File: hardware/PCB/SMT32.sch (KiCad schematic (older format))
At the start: 24 parts, among them J1 USB_B_Micro, SW1 SW_DIP_x01, SW2 SW_DIP_x01, U3 AZ1117CH-3.3, U4 STM32F303CCTx, Y1 X50328MSB2GI

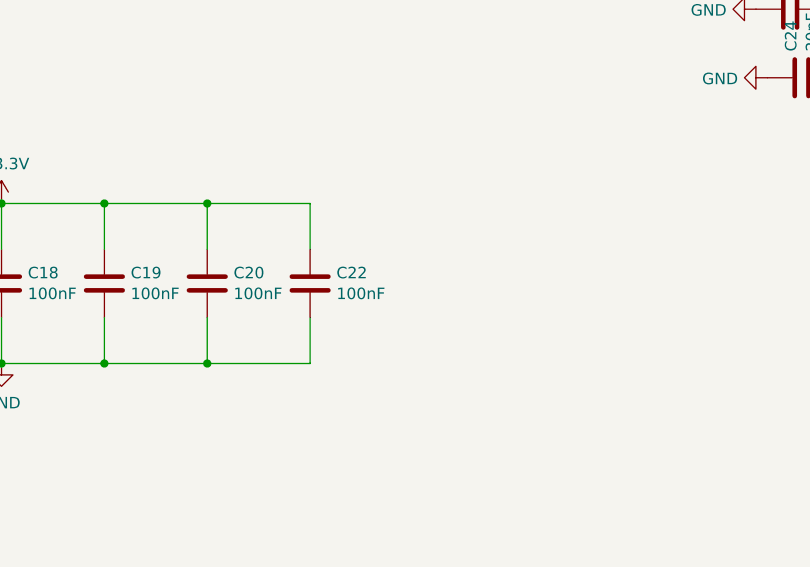
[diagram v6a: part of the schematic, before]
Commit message: Rotate the RGB controller. gonna have a lot of work to do
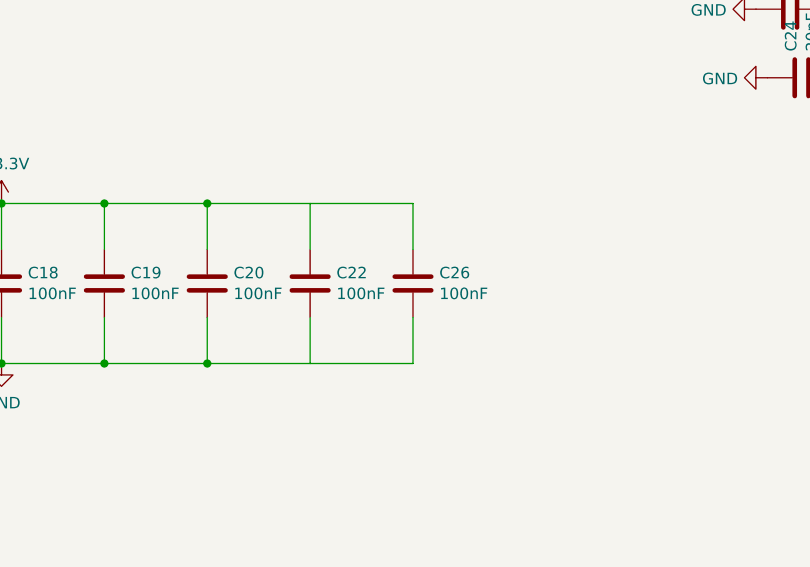
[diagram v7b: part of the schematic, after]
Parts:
- added C26: 100nF, Capacitor_SMD:C_0402_1005Metric, symbol Device:C
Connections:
- net +3V3: now also C26.1
- net GND: now also C26.2
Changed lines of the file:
@@
-$EndComp
-$Comp
-L Device:C C22
-U 1 1 5E14F850
-P 2450 4050
-F 0 "C22" H 2565 4096 50  0000 L CNN
-F 1 "100nF" H 2565 4005 50  0000 L CNN
-F 2 "Capacitor_SMD:C_0402_1005Metric" H 2488 3900 50  0001 C CNN
-F 3 "~" H 2450 4050 50  0001 C CNN
-	1    2450 4050
-	1    0    0    -1
 $EndComp
 $Comp
@@
 Wire Wire Line
 	1100 4400 1550 4400
-Wire Wire Line
-	2450 4400 2450 4200
 Wire Wire Line
 	2000 4400 2000 4200
@@
 	1100 3700 1550 3700
 Wire Wire Line
-	2450 3700 2450 3900
-Wire Wire Line
 	2000 3700 2000 3900
-Connection ~ 2000 3700
-Wire Wire Line
-	2000 3700 2450 3700
 Wire Wire Line
 	1550 3900 1550 3700
@@
 Wire Wire Line
 	2400 6500 1900 6500
+Connection ~ 2000 3700
+Wire Wire Line
+	2000 3700 2450 3700
+Wire Wire Line
+	2450 3700 2450 3900
+Wire Wire Line
+	2450 4400 2450 4200
+$Comp
+L Device:C C22
+U 1 1 5E14F850
+P 2450 4050
+F 0 "C22" H 2565 4096 50  0000 L CNN
+F 1 "100nF" H 2565 4005 50  0000 L CNN
+F 2 "Capacitor_SMD:C_0402_1005Metric" H 2488 3900 50  0001 C CNN
+F 3 "~" H 2450 4050 50  0001 C CNN
+	1    2450 4050
+	1    0    0    -1
+$EndComp
+Wire Wire Line
+	2450 4400 2900 4400
+Wire Wire Line
+	2450 3700 2900 3700
+Wire Wire Line
+	2900 3700 2900 3900
+Wire Wire Line
+	2900 4400 2900 4200
+$Comp
+L Device:C C26
+U 1 1 5E2EDC45
+P 2900 4050
+F 0 "C26" H 3015 4096 50  0000 L CNN
+F 1 "100nF" H 3015 4005 50  0000 L CNN
+F 2 "Capacitor_SMD:C_0402_1005Metric" H 2938 3900 50  0001 C CNN
+F 3 "~" H 2900 4050 50  0001 C CNN
+	1    2900 4050
+	1    0    0    -1
+$EndComp
 $EndSCHEMATC

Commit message: getting closer to it actually works
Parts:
- removed C21: 22uf, Capacitor_SMD:C_0402_1005Metric, symbol Device:C
- added C1: 22μF/10V, Capacitor_Tantalum_SMD:CP_EIA-3216-18_Kemet-A, symbol Device:CP1_Small
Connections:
- net +3V3: now also C1.1
- net GND: now also C1.2
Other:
- note added: "C17, C1 ESR<20Ohm"
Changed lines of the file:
@@
 Wire Wire Line
 	1300 6050 1400 6050
-Wire Wire Line
-	2400 6200 2400 6050
 Connection ~ 2400 6050
 Wire Wire Line
@@
 F 3 "http://www.zlgmcu.com/Sipex/LDO/PDF/spx2920.pdf" H 1900 6000 50  0001 C CNN
 	1    1900 6050
-	1    0    0    -1
-$EndComp
-$Comp
-L Device:C C21
-U 1 1 5E431976
-P 2400 6350
-F 0 "C21" H 2515 6396 50  0000 L CNN
-F 1 "22uf" H 2515 6305 50  0000 L CNN
-F 2 "Capacitor_SMD:C_0402_1005Metric" H 2438 6200 50  0001 C CNN
-F 3 "~" H 2400 6350 50  0001 C CNN
-	1    2400 6350
 	1    0    0    -1
 $EndComp
@@
 	1    0    0    -1
 $EndComp
+$Comp
+L Device:CP1_Small C?
+U 1 1 5E31A107
+P 2400 6400
+AR Path="/5EC33E3D/5E31A107" Ref="C?"  Part="1"
+AR Path="/5E1424B2/5E31A107" Ref="C1"  Part="1"
+F 0 "C1" H 2491 6446 50  0000 L CNN
+F 1 "22μF/10V" H 2491 6355 50  0000 L CNN
+F 2 "Capacitor_Tantalum_SMD:CP_EIA-3216-18_Kemet-A" H 2400 6400 50  0001 C CNN
+F 3 "~" H 2400 6400 50  0001 C CNN
+F 4 "Capacitor_Tantalum_SMD:CP_EIA-3528-12_Kemet-T_Pad1.50x2.35mm_HandSolder" H 2400 6400 50  0001 C CNN "Footprint"
+F 5 "22μF/10V" H 2400 6400 50  0001 C CNN "Value"
+	1    2400 6400
+	1    0    0    -1
+$EndComp
+Wire Wire Line
+	2400 6050 2400 6300
+Text Notes 750  6700 0    50   ~ 0
+C17, C1 ESR<20Ohm
 $EndSCHEMATC
